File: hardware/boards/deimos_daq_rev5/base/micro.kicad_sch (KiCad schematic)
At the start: 91 parts, among them IC1 STM32H743ZIT6, J4 Conn_02x07_Odd_Even, Y1 SiT1602BI-21-33S-48.000000

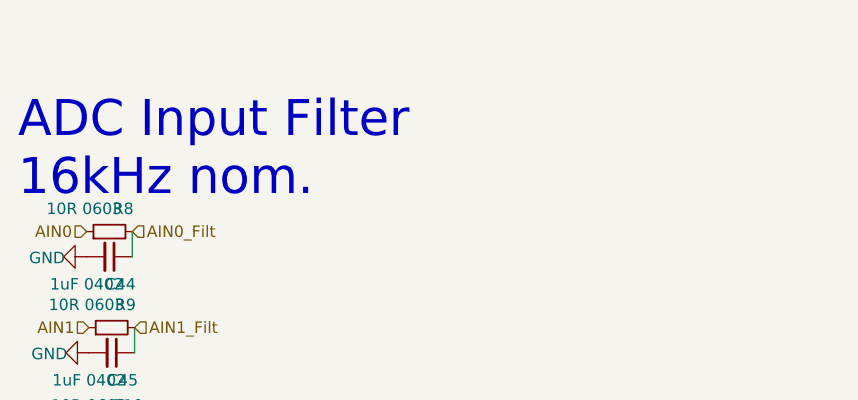
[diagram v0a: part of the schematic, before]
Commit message: fix ldos
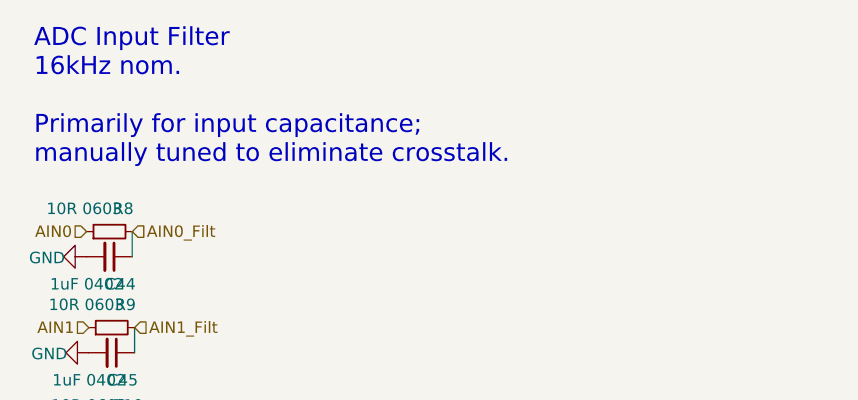
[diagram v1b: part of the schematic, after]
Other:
- note added: "ADC Input Filter 16kHz nom. Primarily for input capacitance; manually tuned to eliminate crosstalk."
- note removed: "ADC Input Filter 16kHz nom."
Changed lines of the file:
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@@
 		)
 	)
-	(text "ADC Input Filter\n16kHz nom."
+	(text "ADC Input Filter\n16kHz nom.\n\nPrimarily for input capacitance;\nmanually tuned to eliminate crosstalk."
 		(exclude_from_sim no)
-		(at 27.94 69.342 0)
+		(at 29.718 65.532 0)
 		(effects
 			(font
-				(size 4 4)
+				(size 2 2)
 			)
 			(justify left bottom)

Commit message: eliminate 5V supply
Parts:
- removed D2002: Purple LED, LED_SMD:LED_0603_1608Metric, symbol Device:LED
- removed R2004: 22.1k 0603, Resistor_SMD:R_0603_1608Metric, symbol Device:R_Small

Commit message: restore rev5 and make this rev rev6
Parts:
- removed D2001, D2003, D2004, D2005: Purple LED, LED_SMD:LED_0603_1608Metric, symbol Device:LED
- removed R2002, R2007, R2008: 10k, Resistor_SMD:R_0402_1005Metric, symbol EK-TM4C1294XL_REV_D-eagle-import:R-US_R0402
- removed R2003: 243k 0603, Resistor_SMD:R_0603_1608Metric, symbol Device:R_Small
- removed R2005, R2006, R2009, R2010: 22.1k 0603, Resistor_SMD:R_0603_1608Metric, symbol Device:R_Small
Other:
- note added: "ADC Input Filter 16kHz nom."
- note removed: "ADC Input Filter 16kHz nom. Primarily for input capacitance; manually tuned to eliminate crosstalk."

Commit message: add more status leds
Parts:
- added D2001, D2002, D2003, D2004, D2005: Purple LED, LED_SMD:LED_0603_1608Metric, symbol Device:LED
- added R2002, R2007, R2008: 10k, Resistor_SMD:R_0402_1005Metric, symbol EK-TM4C1294XL_REV_D-eagle-import:R-US_R0402
- added R2003: 243k 0603, Resistor_SMD:R_0603_1608Metric, symbol Device:R_Small
- added R2004, R2005, R2006, R2009, R2010: 22.1k 0603, Resistor_SMD:R_0603_1608Metric, symbol Device:R_Small
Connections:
- net +3V3: now also R2002.2
- net GND: now also D2001.1 (K), D2002.1 (K), D2003.1 (K), D2004.1 (K), R2008.2
- new net: D2003.2 (A), R2005.1
- new net: D2004.2 (A), R2003.1
- new net: R2005.2, R2006.2
- new net: D2001.2 (A), R2002.1
- new net: D2005.2 (A), R2010.1
- new net: R2008.1, R2009.1
- new net: R2009.2, R2010.2
- new net: D2002.2 (A), R2004.1
- new net: R2006.1, R2007.1
- new net +12V: R2007.2
- new net +24V: R2003.2
- new net +5V: R2004.2
- new net -12V: D2005.1 (K)
